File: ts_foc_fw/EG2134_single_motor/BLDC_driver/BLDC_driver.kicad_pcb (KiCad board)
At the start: 2 copper layers, 3 parts, among them U1 EG2134_N, U2 TPS5430DDAR

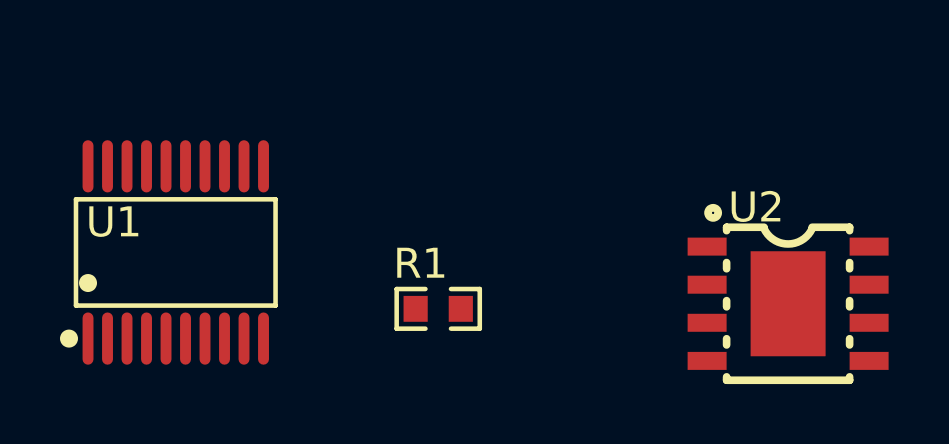
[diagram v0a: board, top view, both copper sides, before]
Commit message: add the cap c0603
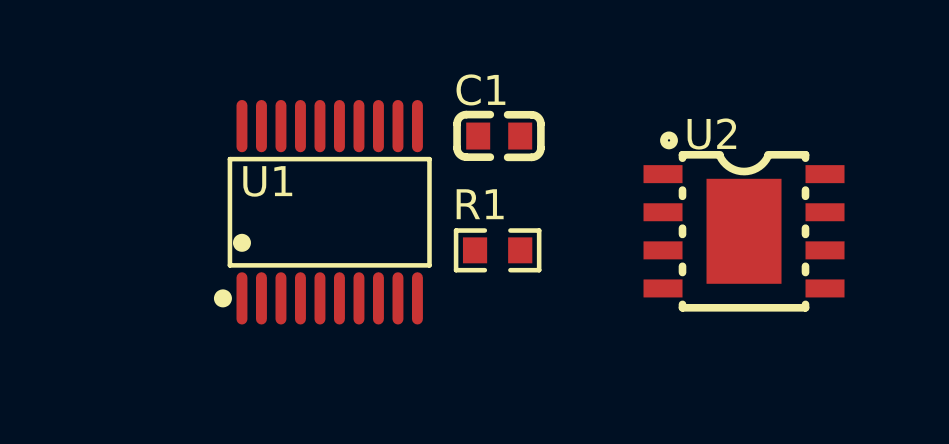
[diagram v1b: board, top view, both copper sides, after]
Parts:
- added C1: 100nf, BLDC_Drive_Tsfoc:C0603, F.Cu at (37.4, 16.5)
- R1: value res -> 10k
- moved U1 5.30 mm to (31.8, 19.1)
- moved U2 2.83 mm to (45.6, 19.7)
- moved R1 2.78 mm to (37.3, 20.3)

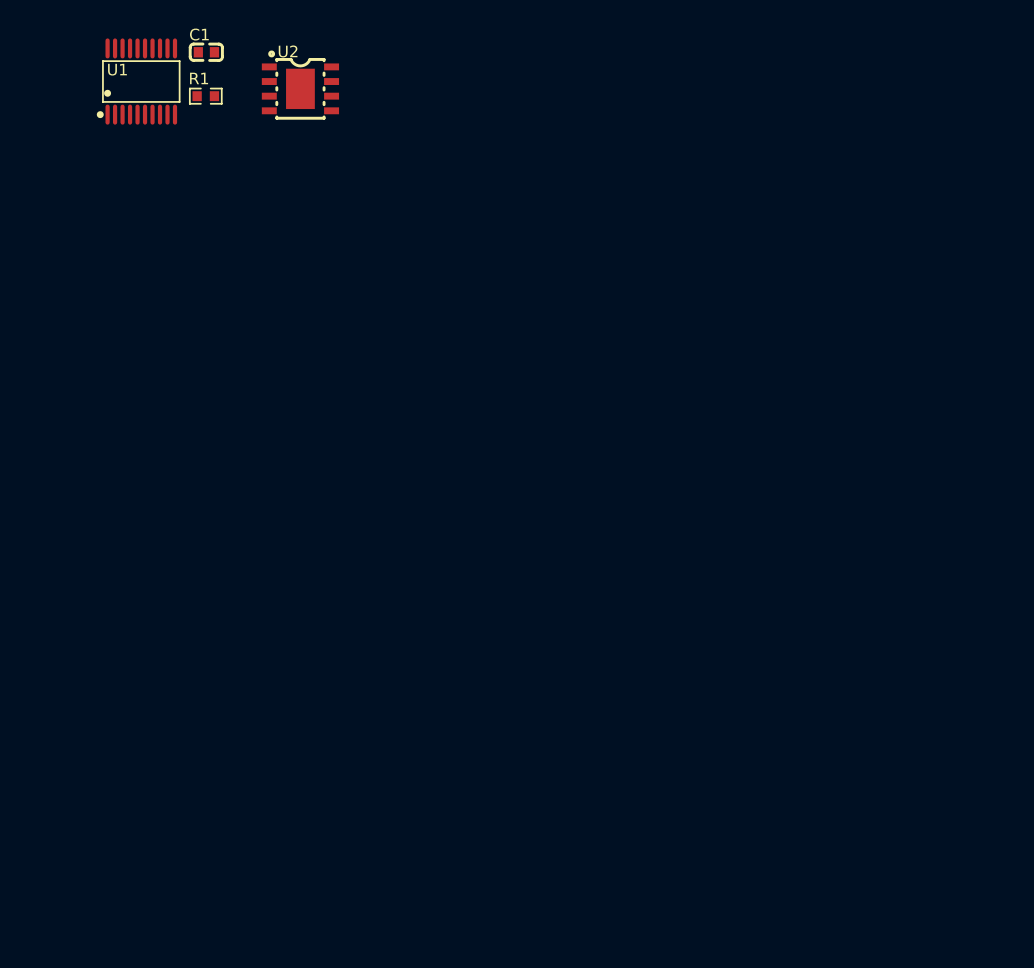
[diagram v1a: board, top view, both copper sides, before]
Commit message: 原理图移植完成,PCB还没有布局
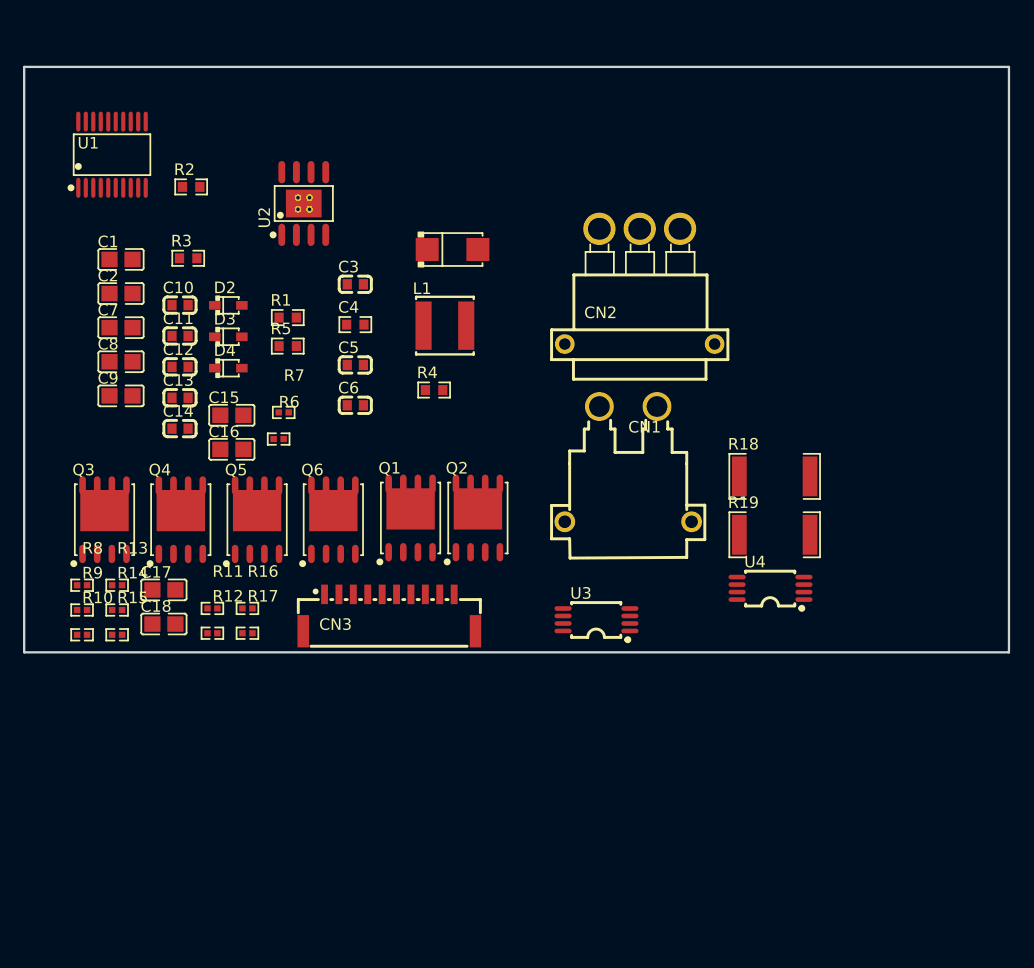
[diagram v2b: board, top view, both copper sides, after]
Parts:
- added C10: 1uf, BLDC_Drive_Tsfoc:C0603, F.Cu at (35.1, 38.5)
- added C11: 100nf, BLDC_Drive_Tsfoc:C0603, F.Cu at (35.1, 41.1)
- added C12: 100nf, BLDC_Drive_Tsfoc:C0603, F.Cu at (35.1, 43.8)
- added C13: 100nf, BLDC_Drive_Tsfoc:C0603, F.Cu at (35.1, 46.5)
- added C14: 100nf, BLDC_Drive_Tsfoc:C0603, F.Cu at (35.1, 49.2)
- added C15: 10uf, BLDC_Drive_Tsfoc:C0805, F.Cu at (39.6, 48.0)
- added C16: 10uf, BLDC_Drive_Tsfoc:C0805, F.Cu at (39.6, 51.0)
- added C17: 10uf, BLDC_Drive_Tsfoc:C0805, F.Cu at (33.7, 63.2)
- added C18: 10uf, BLDC_Drive_Tsfoc:C0805, F.Cu at (33.7, 66.1)
- added C2: 4.7uf, BLDC_Drive_Tsfoc:C0805, F.Cu at (30.0, 37.4)
- added C3: 100nf, BLDC_Drive_Tsfoc:C0603, F.Cu at (50.3, 36.6)
- added C4: 8.2nf, BLDC_Drive_Tsfoc:R0603, F.Cu at (50.3, 40.1)
- added C5: 1.2nf, BLDC_Drive_Tsfoc:C0603, F.Cu at (50.3, 43.6)
- added C6: 10pf, BLDC_Drive_Tsfoc:C0603, F.Cu at (50.3, 47.1)
- added C7: 100nf, BLDC_Drive_Tsfoc:C0805, F.Cu at (30.0, 40.4)
- added C8: 10uf, BLDC_Drive_Tsfoc:C0805, F.Cu at (30.0, 43.4)
- added C9: 10uf, BLDC_Drive_Tsfoc:C0805, F.Cu at (30.0, 46.3)
- added CN1: XT30PW-M, BLDC_Drive_Tsfoc:XT30PW-M30.G.Y, F.Cu at (74.0, 52.2)
- added CN2: MR30PW-M30.G.Y, BLDC_Drive_Tsfoc:MR30PW-M30.G.Y, F.Cu at (75.0, 36.8)
- added CN3: WAFER-GH1.25-10PWB, BLDC_Drive_Tsfoc:WAFER-GH1.25-10PWB, F.Cu at (53.3, 65.2)
- added D1: SS34, BLDC_Drive_Tsfoc:ss34, F.Cu at (58.8, 33.6)
- added D2: 1N5819WS, BLDC_Drive_Tsfoc:1N5819WS, F.Cu at (39.3, 38.5)
- added D3: 1N5819WS, BLDC_Drive_Tsfoc:1N5819WS, F.Cu at (39.3, 41.2)
- added D4: 1N5819WS, BLDC_Drive_Tsfoc:1N5819WS, F.Cu at (39.3, 43.9)
- added L1: SWPA5040S6R8M, BLDC_Drive_Tsfoc:SWPA5040S6R8MT, F.Cu at (58.1, 40.2)
- added Q1: RU3089M-C, BLDC_Drive_Tsfoc:RU3089M-C, F.Cu at (55.1, 56.9)
- added Q2: RU3089M-C, BLDC_Drive_Tsfoc:RU3089M-C, F.Cu at (61.0, 56.9)
- added Q3: RU3089M-C, BLDC_Drive_Tsfoc:RU3089M-C, F.Cu at (28.6, 57.1)
- added Q4: RU3089M-C, BLDC_Drive_Tsfoc:RU3089M-C, F.Cu at (35.2, 57.1)
- added Q5: RU3089M-C, BLDC_Drive_Tsfoc:RU3089M-C, F.Cu at (41.8, 57.1)
- added Q6: RU3089M-C, BLDC_Drive_Tsfoc:RU3089M-C, F.Cu at (48.4, 57.1)
- added R10: 10k, BLDC_Drive_Tsfoc:R0402, F.Cu at (26.6, 67.1)
- added R11: 2.2, BLDC_Drive_Tsfoc:R0402, F.Cu at (37.9, 64.8)
- added R12: 10k, BLDC_Drive_Tsfoc:R0402, F.Cu at (37.9, 66.9)
- added R13: 2.2, BLDC_Drive_Tsfoc:R0402, F.Cu at (29.7, 62.8)
- added R14: 10k, BLDC_Drive_Tsfoc:R0402, F.Cu at (29.7, 64.9)
- added R15: 2.2, BLDC_Drive_Tsfoc:R0402, F.Cu at (29.7, 67.1)
- added R16: 10k, BLDC_Drive_Tsfoc:R0402, F.Cu at (41.0, 64.8)
- added R17: 2.2, BLDC_Drive_Tsfoc:R0402, F.Cu at (41.0, 66.9)
- added R18: res_10r, BLDC_Drive_Tsfoc:R2512, F.Cu at (86.7, 53.3)
- added R19: res_10r, BLDC_Drive_Tsfoc:R2512, F.Cu at (86.7, 58.4)
- added R2: 330k, BLDC_Drive_Tsfoc:R0603, F.Cu at (36.1, 28.2)
- added R3: 68k, BLDC_Drive_Tsfoc:R0603, F.Cu at (35.8, 34.4)
- added R4: 30k, BLDC_Drive_Tsfoc:R0603, F.Cu at (57.2, 45.8)
- added R5: 1.87k, BLDC_Drive_Tsfoc:R0603, F.Cu at (44.5, 42.0)
- added R6: 2.2, BLDC_Drive_Tsfoc:R0402, F.Cu at (43.7, 50.1)
- added R7: 10k, BLDC_Drive_Tsfoc:R0402, F.Cu at (44.1, 47.8)
- added R8: 2.2, BLDC_Drive_Tsfoc:R0402, F.Cu at (26.6, 62.8)
- added R9: 10k, BLDC_Drive_Tsfoc:R0402, F.Cu at (26.6, 64.9)
- added U3: INA240A2PW, BLDC_Drive_Tsfoc:INA240A2PW, F.Cu at (71.2, 65.8)
- added U4: INA240A2PW, BLDC_Drive_Tsfoc:INA240A2PW, F.Cu at (86.3, 63.0)
- C1: value 100nf -> 4.7uf; footprint BLDC_Drive_Tsfoc:C0603 -> BLDC_Drive_Tsfoc:C0805
- U2: value TPS5430DDAR -> TPS54331DDAR; footprint BLDC_Drive_Tsfoc:tps5430 -> BLDC_Drive_Tsfoc:tps54331
- moved R1 20.5 mm to (44.5, 39.5)
- moved C1 19.4 mm to (30.0, 34.5)
- moved U2 9.95 mm to (45.8, 29.6)
- moved U1 6.84 mm to (29.2, 25.4)
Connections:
- C1 pad 1: unconnected-(C1-Pad1) -> GND
- C1 pad 2: unconnected-(C1-Pad2) -> +12V
- R1 pad 1: unconnected-(R1-Pad1) -> Net-(U2-VSENSE)
- R1 pad 2: unconnected-(R1-Pad2) -> +5V
- U1 pad 1: unconnected-(U1-HIN1-Pad1) -> /EG2134栅极驱动/M0_IN1
- U1 pad 10: unconnected-(U1-LO2-Pad10) -> /EG2134栅极驱动/M0_GL2
- U1 pad 11: unconnected-(U1-LO1-Pad11) -> /EG2134栅极驱动/M0_GL1
- U1 pad 12: unconnected-(U1-VS3-Pad12) -> /EG2134栅极驱动/M0_OUT3
- U1 pad 13: unconnected-(U1-HO3-Pad13) -> /EG2134栅极驱动/M0_GH3
- U1 pad 14: unconnected-(U1-VB3-Pad14) -> Net-(D4-K)
- U1 pad 15: unconnected-(U1-VS2-Pad15) -> /EG2134栅极驱动/M0_OUT2_P
- U1 pad 16: unconnected-(U1-HO2-Pad16) -> /EG2134栅极驱动/M0_GH2
- U1 pad 17: unconnected-(U1-VB2-Pad17) -> Net-(D3-K)
- U1 pad 18: unconnected-(U1-VS1-Pad18) -> /EG2134栅极驱动/M0_OUT1_P
- U1 pad 19: unconnected-(U1-HO1-Pad19) -> /EG2134栅极驱动/M0_GH1
- U1 pad 2: unconnected-(U1-HIN2-Pad2) -> /EG2134栅极驱动/M0_IN2
- U1 pad 20: unconnected-(U1-VB1-Pad20) -> Net-(D2-K)
- U1 pad 3: unconnected-(U1-HIN3-Pad3) -> /EG2134栅极驱动/M0_IN3
- U1 pad 4: unconnected-(U1-LIN1-Pad4) -> /EG2134栅极驱动/M0_IN1
- U1 pad 5: unconnected-(U1-LIN2-Pad5) -> /EG2134栅极驱动/M0_IN2
- U1 pad 6: unconnected-(U1-LIN3-Pad6) -> /EG2134栅极驱动/M0_IN3
- U1 pad 7: unconnected-(U1-VCC-Pad7) -> Net-(U1-VCC)
- U1 pad 8: unconnected-(U1-GND-Pad8) -> GND
- U1 pad 9: unconnected-(U1-LO3-Pad9) -> /EG2134栅极驱动/M0_GL3
- U2 pad 1: unconnected-(U2-BOOT-Pad1) -> Net-(U2-BOOT)
- U2 pad 2: unconnected-(U2-NC-Pad2) -> +12V
- U2 pad 3: unconnected-(U2-NC-Pad3) -> Net-(U2-EN)
- U2 pad 4: unconnected-(U2-VSENSE-Pad4) -> Net-(U2-SS)
- U2 pad 5: unconnected-(U2-ENA-Pad5) -> Net-(U2-VSENSE)
- U2 pad 6: unconnected-(U2-GND-Pad6) -> Net-(U2-COMP)
- U2 pad 7: unconnected-(U2-VIN-Pad7) -> GND
- U2 pad 8: unconnected-(U2-PH-Pad8) -> Net-(D1-K)
- U2 pad 9: unconnected-(U2-PowerPAD-Pad9) -> GND
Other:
- board outline added: 85.5 x 50.8 mm

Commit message: dayly
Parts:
- C4: footprint BLDC_Drive_Tsfoc:R0603 -> BLDC_Drive_Tsfoc:C0603
- U1: footprint BLDC_Drive_Tsfoc:EG2134_N_TSSOP-20_L6.5-W4.4-P0.65-LS6.4-BL -> BLDC_Drive_Tsfoc:EG2134
- moved R2 48.3 mm to (76.2, 55.1)
- moved R3 46.6 mm to (76.2, 57.6)
- moved C1 45.6 mm to (71.7, 52.9)
- moved C2 45.6 mm to (71.7, 55.9)
- moved C7 45.6 mm to (71.7, 58.8)
- moved C8 45.6 mm to (71.7, 61.8)
- moved C9 45.6 mm to (71.7, 64.7)
- moved U2 44.2 mm to (81.6, 55.6)
- moved D1 43.9 mm to (85.9, 68.1)
- moved CN2 41.5 mm to (44.4, 64.8)
- moved C3 38.6 mm to (80.2, 61.1)
- moved C4 38.1 mm to (80.2, 63.8)
- moved R10 37.9 mm to (49.8, 37.1)
- moved R5 37.8 mm to (76.2, 62.6)
- moved C5 37.6 mm to (80.2, 66.5)
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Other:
- board size 85.5 x 50.8 mm -> 85.5 x 76 mm

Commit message: PCB_layout_ing
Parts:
- added R20: 0, BLDC_Drive_Tsfoc:R0805, F.Cu at (36.8, 58.5)
- C10, C11, C15, C16, D2, D3, D4, R6, R7: moved to B.Cu
- R18, R19: value res_10r -> 10mr
- moved U4 59.8 mm to (48.6, 29.9), turned to 90 degrees
- moved U3 58.9 mm to (43.9, 29.9), turned to 90 degrees
- moved R15 48.9 mm to (33.6, 84.2)
- moved R14 48.9 mm to (33.6, 82.1)
- moved R16 48.9 mm to (33.6, 86.4)
- moved R17 48.9 mm to (33.6, 88.5)
- moved R19 48.1 mm to (49.4, 38.6), turned to 90 degrees
- moved R18 48.0 mm to (41.8, 39.2), turned to -90 degrees
- moved R10 46.9 mm to (37.5, 82.3)
- moved R12 46.9 mm to (37.5, 86.6)
- moved R13 46.9 mm to (37.5, 88.8)
- moved R11 46.9 mm to (37.5, 84.5)
- moved Q2 45.4 mm to (84.4, 56.0), turned to 90 degrees
- moved CN1 45.2 mm to (98.9, 41.8), turned to 90 degrees
- moved C6 44.9 mm to (84.8, 24.5), turned to -90 degrees
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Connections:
- net /EG2134栅极驱动/M0_GH1 renamed M0_GH1
- net /EG2134栅极驱动/M0_GH2 renamed M0_GH2
- net /EG2134栅极驱动/M0_GH3 renamed M0_GH3
- net /EG2134栅极驱动/M0_GL1 renamed M0_GL1
- net /EG2134栅极驱动/M0_GL2 renamed M0_GL2
- net /EG2134栅极驱动/M0_GL3 renamed M0_GL3
- net /EG2134栅极驱动/M0_IN1 renamed M0_IN1
- net /EG2134栅极驱动/M0_IN2 renamed M0_IN2
- net /EG2134栅极驱动/M0_IN3 renamed M0_IN3
- C12 pad 1: /EG2134栅极驱动/M0_OUT1_P -> M0_OUT1_P
- C13 pad 1: /EG2134栅极驱动/M0_OUT2_P -> M0_OUT2_P
- C14 pad 1: /EG2134栅极驱动/M0_OUT3 -> M0_OUT3
- CN2 pad 1: /Connection/M0_OUT3 -> M0_OUT3
- CN2 pad 2: /Connection/M0_OUT2_N -> M0_OUT2_N
- CN2 pad 3: /Connection/M0_OUT1_N -> M0_OUT1_N
- CN3 pad 10: /Connection/M0_OUT1_CS -> M0_OUT1_CS
- CN3 pad 9: /Connection/M0_OUT2_CS -> M0_OUT2_CS
- Q1 pad 1: /EG2134栅极驱动/M0_OUT1_P -> M0_OUT1_P
- Q1 pad 2: /EG2134栅极驱动/M0_OUT1_P -> M0_OUT1_P
- Q1 pad 3: /EG2134栅极驱动/M0_OUT1_P -> M0_OUT1_P
- Q2 pad 5: Net-(Q2-D-Pad5) -> M0_OUT1_P
- Q2 pad 6: Net-(Q2-D-Pad5) -> M0_OUT1_P
- Q2 pad 7: Net-(Q2-D-Pad5) -> M0_OUT1_P
- Q2 pad 8: Net-(Q2-D-Pad5) -> M0_OUT1_P
- Q2 pad 9: /EG2134栅极驱动/M0_OUT1_P -> M0_OUT1_P
- Q3 pad 1: /EG2134栅极驱动/M0_OUT2_P -> M0_OUT2_P
- Q3 pad 2: /EG2134栅极驱动/M0_OUT2_P -> M0_OUT2_P
- Q3 pad 3: /EG2134栅极驱动/M0_OUT2_P -> M0_OUT2_P
- Q4 pad 5: Net-(Q4-D-Pad5) -> M0_OUT2_P
- Q4 pad 6: Net-(Q4-D-Pad5) -> M0_OUT2_P
- Q4 pad 7: Net-(Q4-D-Pad5) -> M0_OUT2_P
- Q4 pad 8: Net-(Q4-D-Pad5) -> M0_OUT2_P
- Q4 pad 9: /EG2134栅极驱动/M0_OUT2_P -> M0_OUT2_P
- Q5 pad 1: /EG2134栅极驱动/M0_OUT3 -> M0_OUT3
- Q5 pad 2: /EG2134栅极驱动/M0_OUT3 -> M0_OUT3
- Q5 pad 3: /EG2134栅极驱动/M0_OUT3 -> M0_OUT3
- Q6 pad 5: Net-(Q6-D-Pad5) -> M0_OUT3
- Q6 pad 6: Net-(Q6-D-Pad5) -> M0_OUT3
- Q6 pad 7: Net-(Q6-D-Pad5) -> M0_OUT3
- Q6 pad 8: Net-(Q6-D-Pad5) -> M0_OUT3
- Q6 pad 9: /EG2134栅极驱动/M0_OUT3 -> M0_OUT3
- R12 pad 1: /EG2134栅极驱动/M0_OUT2_P -> M0_OUT2_P
- R16 pad 1: /EG2134栅极驱动/M0_OUT3 -> M0_OUT3
- R18 pad 1: /cirrent_sensor/M0_OUT1_P -> M0_OUT1_P
- R18 pad 2: /cirrent_sensor/M0_OUT1_N -> M0_OUT1_N
- R19 pad 1: /cirrent_sensor/M0_OUT2_P -> M0_OUT2_P
- R19 pad 2: /cirrent_sensor/M0_OUT2_N -> M0_OUT2_N
- R7 pad 1: /EG2134栅极驱动/M0_OUT1_P -> M0_OUT1_P
- U1 pad 12: /EG2134栅极驱动/M0_OUT3 -> M0_OUT3
- U1 pad 15: /EG2134栅极驱动/M0_OUT2_P -> M0_OUT2_P
- U1 pad 18: /EG2134栅极驱动/M0_OUT1_P -> M0_OUT1_P
- U3 pad 2: /cirrent_sensor/M0_OUT1_N -> M0_OUT1_N
- U3 pad 3: /cirrent_sensor/M0_OUT1_P -> M0_OUT1_P
- U3 pad 8: /cirrent_sensor/M0_OUT1_CS -> M0_OUT1_CS
- U4 pad 2: /cirrent_sensor/M0_OUT2_N -> M0_OUT2_N
- U4 pad 3: /cirrent_sensor/M0_OUT2_P -> M0_OUT2_P
- U4 pad 8: /cirrent_sensor/M0_OUT2_CS -> M0_OUT2_CS

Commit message: 同步
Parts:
- C17, C18, R12, R13, R16, R17: moved to B.Cu
- moved R17 59.3 mm to (49.5, 31.4), turned to 180 degrees
- moved R16 58.3 mm to (49.5, 30.3)
- moved R15 54.4 mm to (40.5, 30.2)
- moved R14 53.5 mm to (40.5, 29.0), turned to 180 degrees
- moved R13 53.4 mm to (49.5, 36.8), turned to 180 degrees
- moved R12 52.4 mm to (49.5, 35.6)
- moved R9 51.5 mm to (40.4, 39.8), turned to 0 degrees
- moved R8 50.8 mm to (40.4, 41.0), turned to 180 degrees
- moved R11 49.0 mm to (40.3, 35.6)
- moved R10 48.0 mm to (40.4, 34.4), turned to 180 degrees
- moved Q2 42.4 mm to (45.5, 39.0), turned to -90 degrees
- moved C18 42.0 mm to (53.4, 36.2), turned to -90 degrees
- moved C17 40.1 mm to (55.4, 36.2), turned to -90 degrees
- moved Q3 37.7 mm to (53.5, 33.7), turned to -90 degrees
- moved R7 33.5 mm to (49.6, 40.9), turned to 0 degrees
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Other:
- board size 85.5 x 76 mm -> 68.9 x 31.5 mm

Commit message: 同步20241108_night
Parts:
- added C19: 4.7uf, BLDC_Drive_Tsfoc:C0805, F.Cu at (77.0, 31.0)
- added C20: 100nf, BLDC_Drive_Tsfoc:C0603, F.Cu at (71.0, 28.5)
- added C21: 100nf, BLDC_Drive_Tsfoc:C0603, F.Cu at (67.5, 33.3)
- added C22: 4.7uf, BLDC_Drive_Tsfoc:C0805, F.Cu at (67.5, 29.5)
- added U5: AMS1117-3.3(SOT-89), BLDC_Drive_Tsfoc:AMS11173v3-SOT-89, F.Cu at (71.9, 32.0)
- moved U3 8.01 mm to (50.9, 26.4)
- moved R18 7.72 mm to (43.0, 26.1)
- moved R19 7.72 mm to (42.9, 22.0)
- moved C14 4.27 mm to (65.8, 25.7)
- moved C12 4.27 mm to (59.7, 25.7)
- moved C13 4.27 mm to (62.7, 25.7)
- moved D3 4.27 mm to (62.6, 25.7)
- moved D2 4.27 mm to (60.8, 25.7)
- moved D4 4.27 mm to (64.5, 25.7)
- moved C11 4.27 mm to (61.8, 37.3)
- moved U1 4.27 mm to (62.8, 31.8)
- moved C10 4.27 mm to (63.6, 37.3)
- moved R14 3.56 mm to (40.5, 32.6)
- moved R15 3.56 mm to (40.5, 33.8)
- moved C15 3.56 mm to (54.0, 45.3)
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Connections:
- CN3 pad 6: GND -> M0_IN3
- CN3 pad 7: GND -> M0_IN2
- CN3 pad 8: GND -> M0_IN1
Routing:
- net +12V: track 0.00 -> 24.2 mm, vias 0 -> 2
- net Net-(D1-K): track 0.00 -> 16.9 mm, vias 0 -> 2
- net Net-(U2-VSENSE): track 0.00 -> 11.3 mm, vias 0 -> 2
- net +5V: track 0.00 -> 6.71 mm
- net Net-(U2-EN): track 0.00 -> 5.84 mm
- net Net-(U2-COMP): track 0.00 -> 4.54 mm
- net PGND: track 0.00 -> 4.18 mm
- net Net-(U2-SS): track 0.00 -> 2.59 mm
- net Net-(U2-BOOT): track 0.00 -> 2.27 mm
- net GND: vias 0 -> 1
- added copper zone on B.Cu, net GND
- added copper zone on F.Cu, net GND
